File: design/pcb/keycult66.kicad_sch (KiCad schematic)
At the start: 181 parts, among them SW1 r0c0 Esc, SW10 r0c9 6, SW11 r0c10 7, SW12 r0c11 8, SW13 r0c12 9, SW14 r0c13 0, SW15 r0c14 Bksp, SW16 r1c0 Tab, SW17 r1c1 Q, SW18 r1c2 W, SW19 r1c3 E, SW2 r0c1 1, SW20 r1c4 R, SW21 r1c5 T, SW22 r1c9 Y, SW23 r1c10 U, SW24 r1c11 I, SW25 r1c12 O, SW26 r1c13 P, SW27 r1c14 \, SW28 r2c0 Caps, SW29 r2c1 A, SW3 r0c2 2, SW30 r2c2 S, SW31 r2c3 D, SW32 r2c4 F, SW33 r2c5 G, SW34 r2c9 H, SW35 r2c10 J, SW36 r2c11 K, SW37 r2c12 L, SW38 r2c13 ;, SW39 r2c14 Enter, SW4 r0c3 3, SW40 r3c0 Shift, SW41 r3c1 Z, SW42 r3c2 X, SW43 r3c3 C, SW44 r3c4 V, SW45 r3c5 B, SW46 r3c9 N, SW47 r3c10 M, SW48 r3c11 ,, SW49 r3c12 ., SW5 r0c4 4, SW50 r3c13 /, SW51 r3c14 Shift, SW52 r4c0 Ctrl, SW53 r4c1 GUI, SW54 r4c2 Alt, SW55 r4c3 Fn, SW56 r4c4 Space, SW57 r4c5 Del, SW58 r4c6 M1, SW59 r4c7 M3, SW6 r0c5 5, SW60 r4c8 M2, SW61 r4c9 Bksp, SW62 r4c10 Space, SW63 r4c11 Fn, SW64 r4c12 Left, SW65 r4c13 Down, SW66 r4c14 Right, SW67 BOOTSEL, SW68 RESET, SW7 r0c6 Vol-, SW8 r0c7 Mute, SW9 r0c8 Vol+, U1 RP2040, U2 W25Q16JVSSIQ, U3 AP2112K-3.3TRG1, Y1 ABM8-272-T3 12MHz CL10pF

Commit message: feat(pcb): complete internal routing for 66-key and 63-key variants
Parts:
- F1: footprint Fuse:Fuse_1206_3216Metric -> Fuse:Fuse_0805_2012Metric
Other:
- note added: "66 keys; stable references from preferred.keys. Central reservation is NOT A HOLE."
- note removed: "66 keys; IDs from preferred.keys; missing r1..3 c6..8 are intentional. Central 50x50mm is RESERVED, NOT A HOLE."

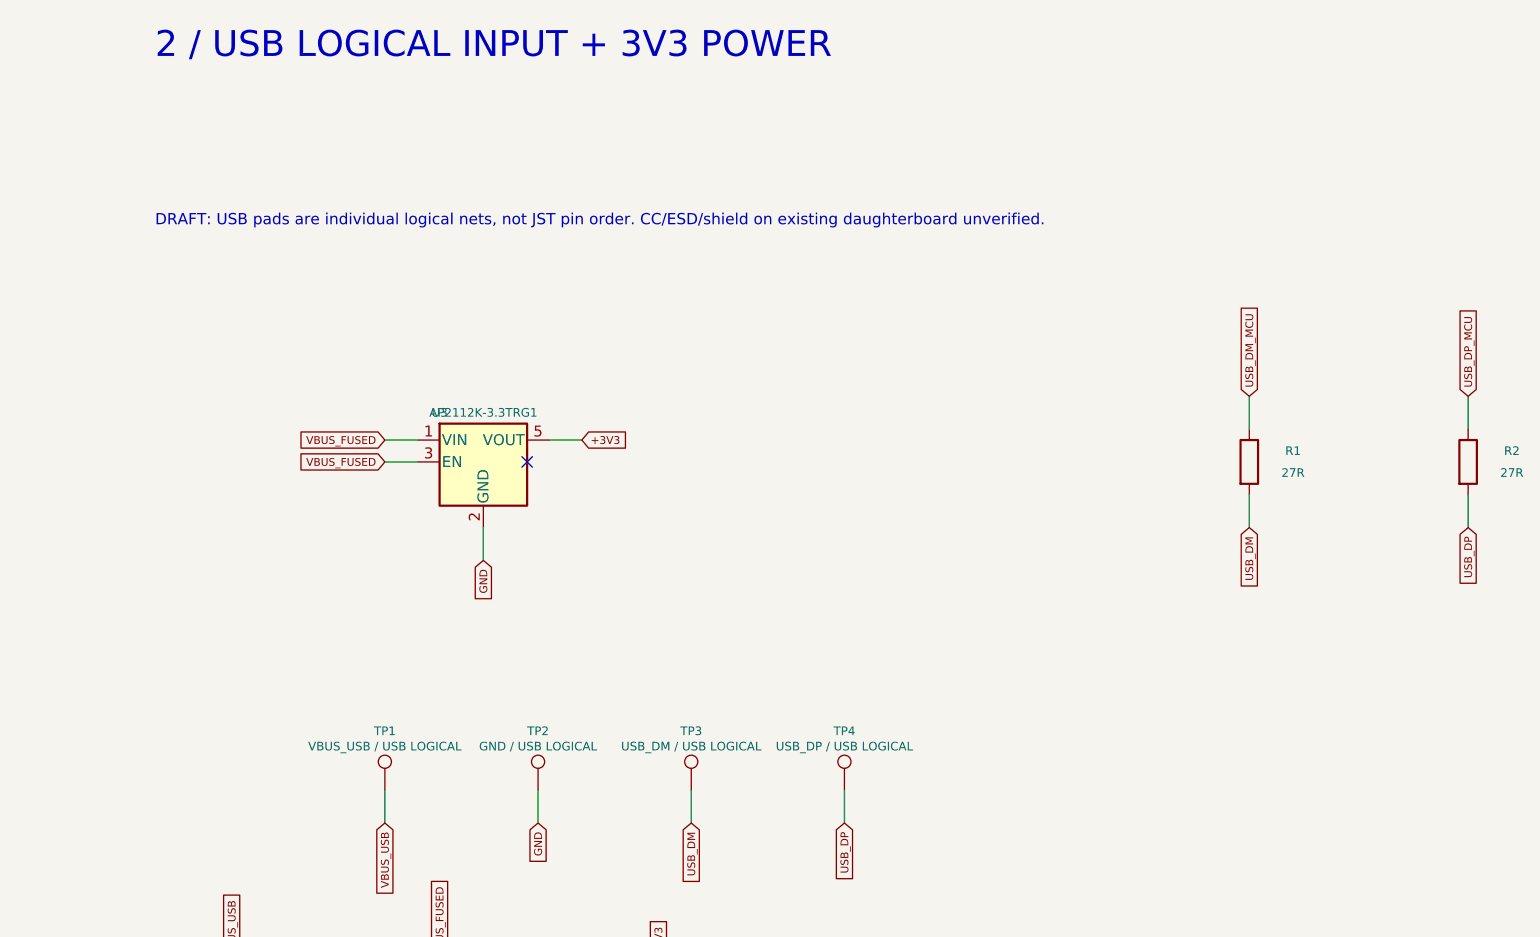
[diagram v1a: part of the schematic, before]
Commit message: feat(pcb): add UDB interface and record paused design checkpoint
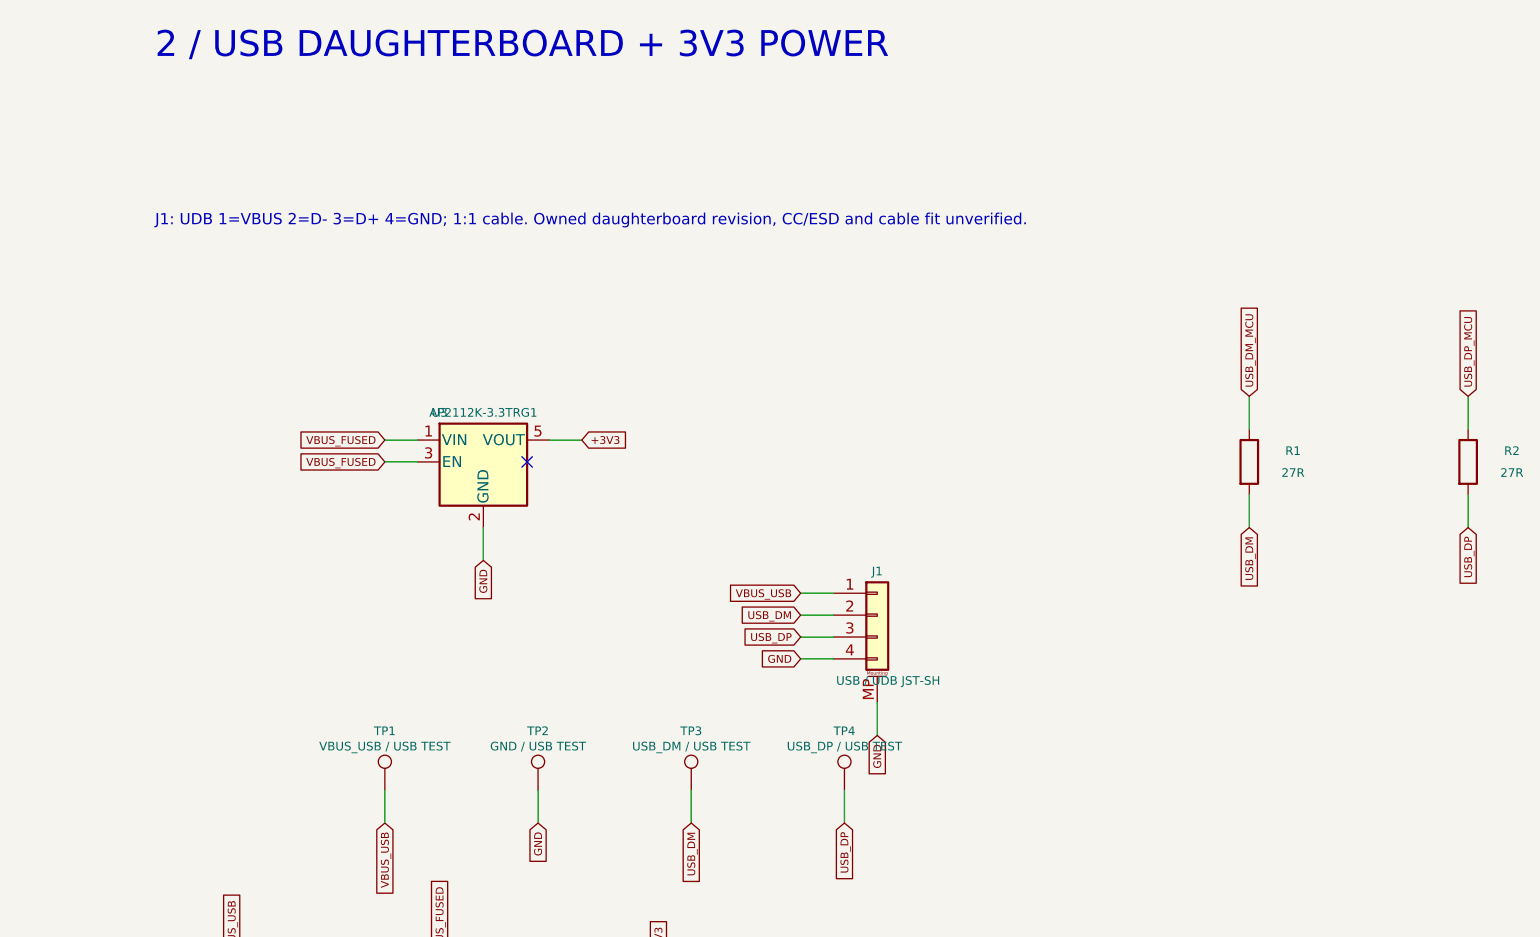
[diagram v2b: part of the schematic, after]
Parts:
- added J1: USB / UDB JST-SH, Connector_JST:JST_SH_SM04B-SRSS-TB_1x04-1MP_P1.00mm_Horizontal, symbol Connector_Generic_MountingPin:Conn_01x04_MountingPin
- TP1: value VBUS_USB / USB LOGICAL -> VBUS_USB / USB TEST
- TP2: value GND / USB LOGICAL -> GND / USB TEST
- TP3: value USB_DM / USB LOGICAL -> USB_DM / USB TEST
- TP4: value USB_DP / USB LOGICAL -> USB_DP / USB TEST
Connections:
- net GND: now also J1.4 (Pin_4), J1.MP (MountPin)
- net USB_DM: now also J1.2 (Pin_2)
- net USB_DP: now also J1.3 (Pin_3)
- net VBUS_USB: now also J1.1 (Pin_1)
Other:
- note added: "2 / USB DAUGHTERBOARD + 3V3 POWER"
- note added: "J1: UDB 1=VBUS 2=D- 3=D+ 4=GND; 1:1 cable. Owned daughterboard revision, CC/ESD and cable fit unverified."
- note removed: "2 / USB LOGICAL INPUT + 3V3 POWER"
- note removed: "DRAFT: USB pads are individual logical nets, not JST pin order. CC/ESD/shield on existing daughterboard unverified."

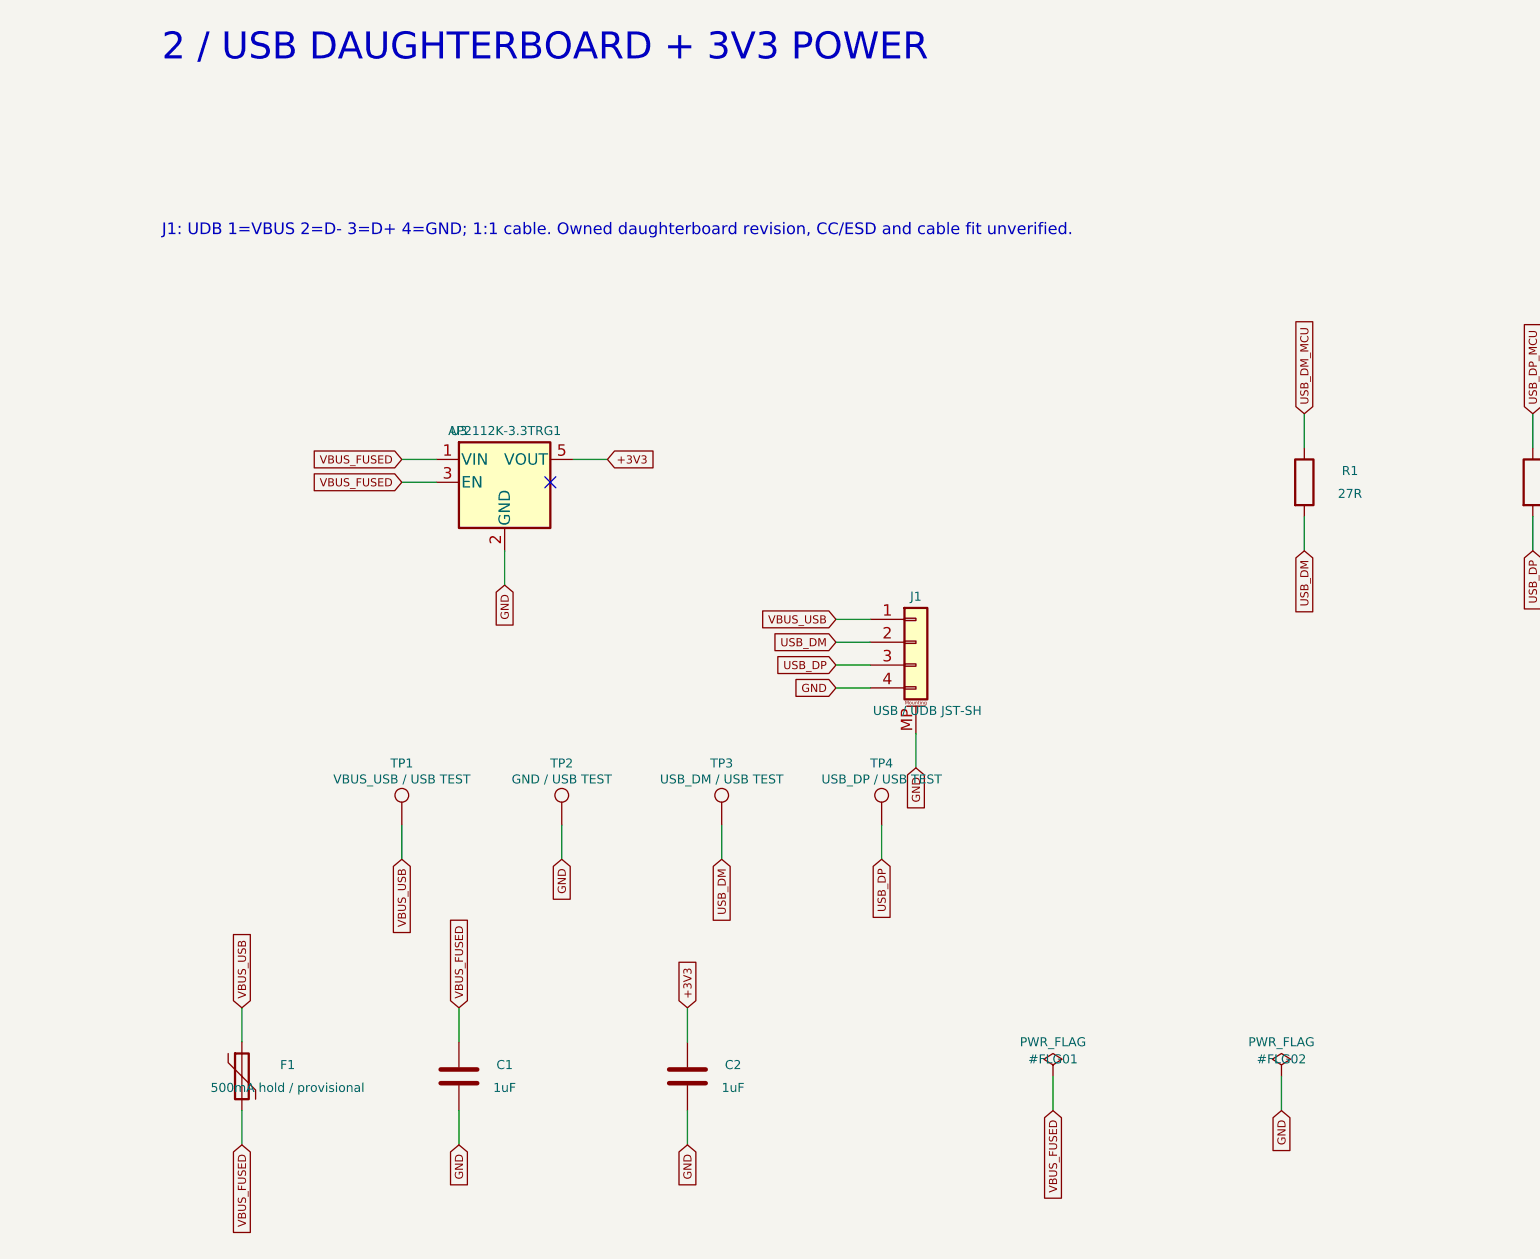
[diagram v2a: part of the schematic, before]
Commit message: feat(pcb): adopt external C5-JSH daughterboard assumption
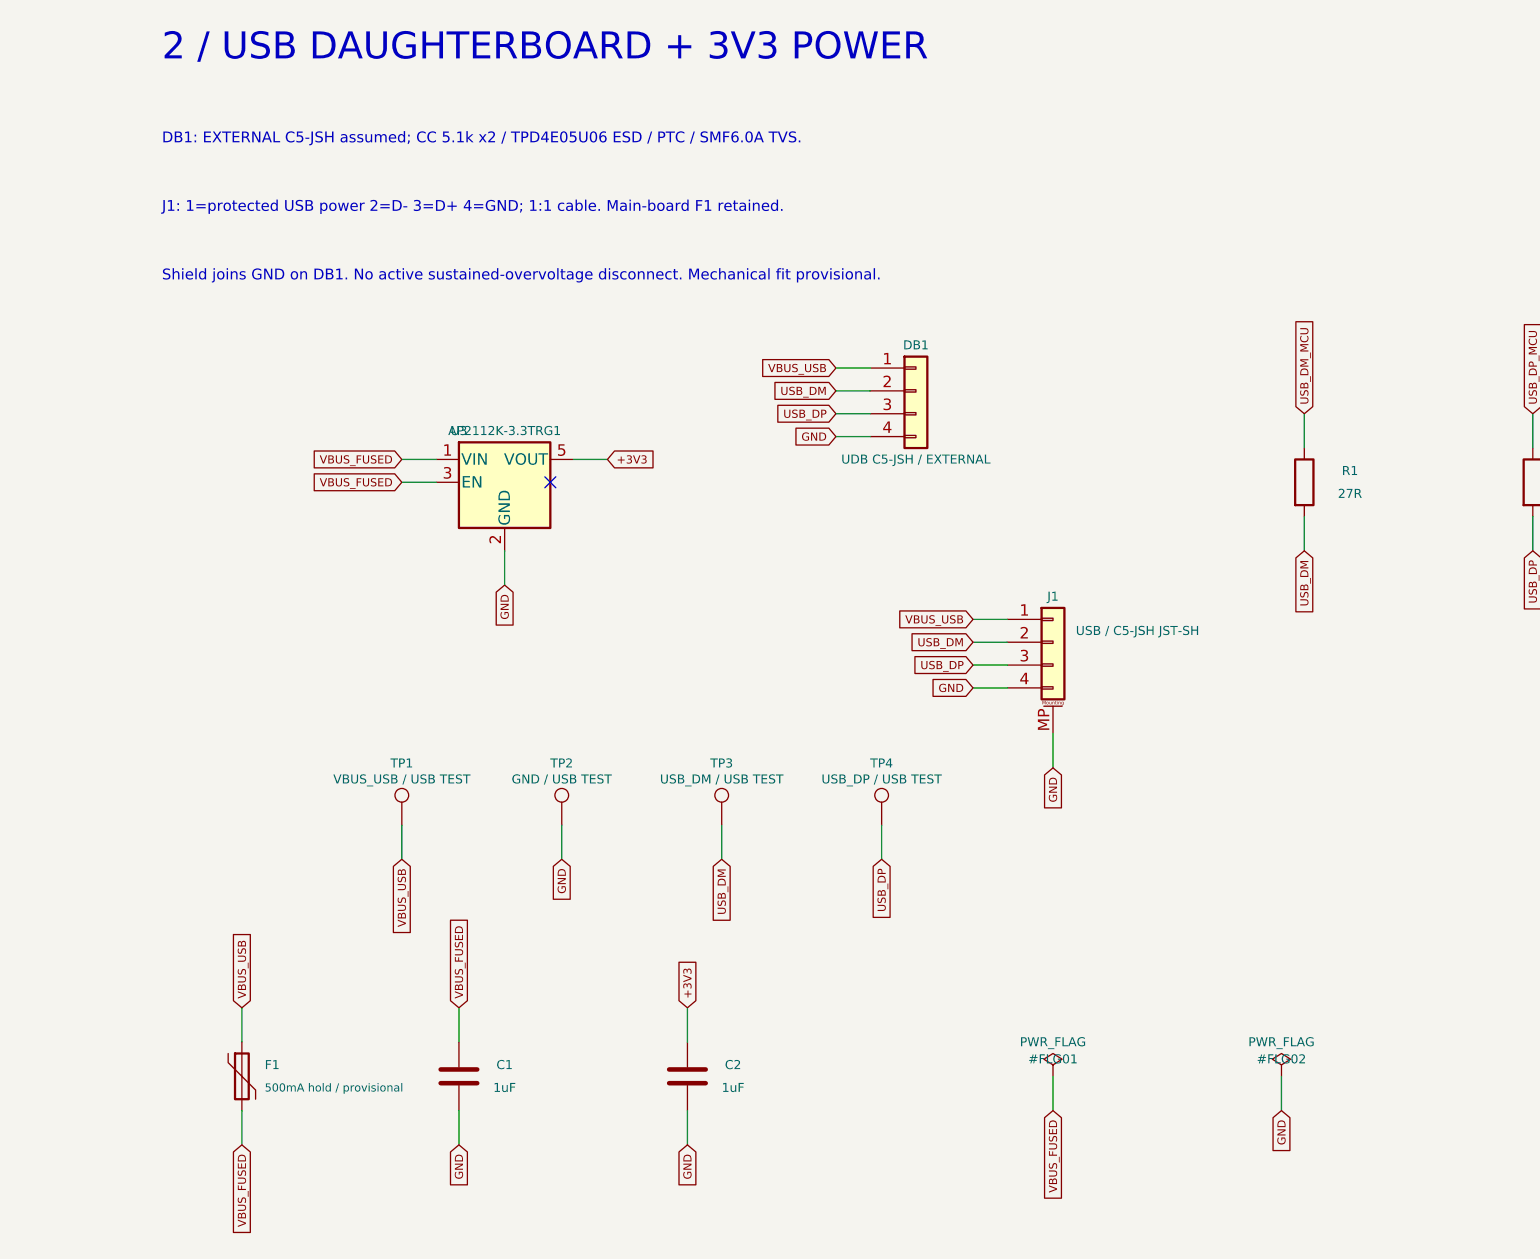
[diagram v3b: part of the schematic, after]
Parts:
- added DB1: UDB C5-JSH / EXTERNAL, symbol Connector_Generic:Conn_01x04
- J1: value USB / UDB JST-SH -> USB / C5-JSH JST-SH
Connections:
- net GND: now also DB1.4 (Pin_4)
- net USB_DM: now also DB1.2 (Pin_2)
- net USB_DP: now also DB1.3 (Pin_3)
- net VBUS_USB: now also DB1.1 (Pin_1)
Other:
- note added: "DB1: EXTERNAL C5-JSH assumed; CC 5.1k x2 / TPD4E05U06 ESD / PTC / SMF6.0A TVS."
- note added: "J1: 1=protected USB power 2=D- 3=D+ 4=GND; 1:1 cable. Main-board F1 retained."
- note added: "Shield joins GND on DB1. No active sustained-overvoltage disconnect. Mechanical fit provisional."
- note removed: "J1: UDB 1=VBUS 2=D- 3=D+ 4=GND; 1:1 cable. Owned daughterboard revision, CC/ESD and cable fit unverified."
- moved on the sheet: J1

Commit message: feat(pcb): use two 1.5u trackball buttons in both layouts
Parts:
- removed D59: 1N4148W, Diode_SMD:D_SOD-123, symbol Device:D
- removed SW59: r4c7 M3, Button_Switch_Keyboard:SW_Cherry_MX_1.00u_PCB, symbol Switch:SW_Push
- SW58, SW60: footprint Button_Switch_Keyboard:SW_Cherry_MX_1.00u_PCB -> Button_Switch_Keyboard:SW_Cherry_MX_1.50u_PCB
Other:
- note added: "65 keys; legacy Keycult66 references. Bottom M1/M2: 1.5u each. Central reservation is NOT A HOLE."
- note removed: "66 keys; stable references from preferred.keys. Central reservation is NOT A HOLE."
